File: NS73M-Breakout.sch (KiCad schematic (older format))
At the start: 5 parts, among them P1 HEADER, P2 RF_OUT, U1 NS73M, Y1 32.768 KHz

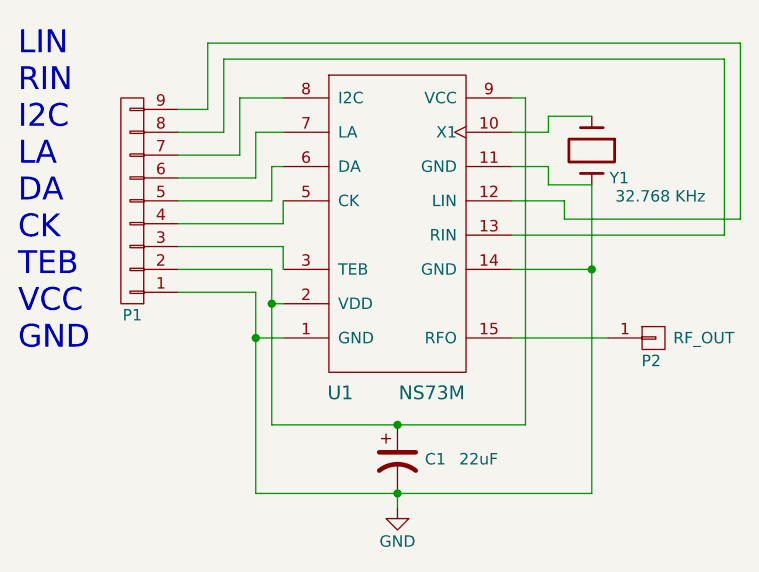
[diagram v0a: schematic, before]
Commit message: Power flags, schematic passes ERC
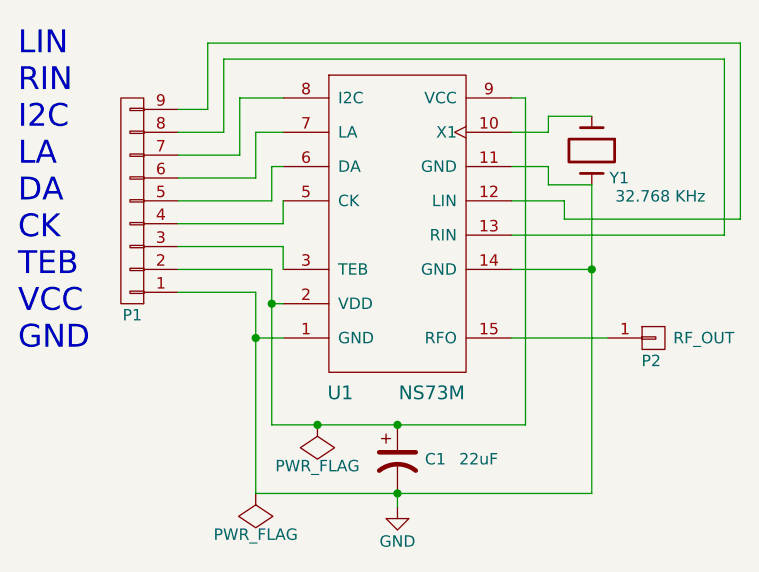
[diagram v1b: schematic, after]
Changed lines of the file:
@@
 	5050 3990 5460 3990
 Wire Wire Line
-	5460 3990 5460 4140
-Wire Wire Line
-	5460 4140 5460 4670
+	5460 3990 5460 4670
 Wire Wire Line
 	5460 4140 5510 4140
@@
 	5050 4090 5390 4090
 Wire Wire Line
-	5390 4090 5390 4290
-Wire Wire Line
-	5390 4290 5390 4970
+	5390 4090 5390 4970
 Wire Wire Line
 	5390 4290 5510 4290
 $Comp
-L GND #PWR1
+L GND #PWR01
 U 1 1 59090A59
 P 6010 5030
-F 0 "#PWR1" H 6010 4780 50  0001 C CNN
+F 0 "#PWR01" H 6010 4780 50  0001 C CNN
 F 1 "GND" H 6010 4880 50  0000 C CNN
 F 2 "" H 6010 5030 50  0000 C CNN
@@
 	6510 3990 6860 3990
 Wire Wire Line
-	6860 4970 6860 3990
-Wire Wire Line
-	6860 3990 6860 3620
+	6860 3620 6860 4970
 Connection ~ 6860 3990
 Wire Wire Line
-	5390 4970 6010 4970
-Wire Wire Line
-	6010 4970 6860 4970
-Wire Wire Line
-	5460 4670 6010 4670
-Wire Wire Line
-	6010 4670 6570 4670
+	6860 4970 5390 4970
 Connection ~ 6010 4670
 Wire Wire Line
@@
 	6010 5030 6010 4970
 Connection ~ 6010 4970
+$Comp
+L PWR_FLAG #FLG02
+U 1 1 590943D2
+P 5660 4670
+F 0 "#FLG02" H 5660 4765 50  0001 C CNN
+F 1 "PWR_FLAG" H 5660 4850 50  0000 C CNN
+F 2 "" H 5660 4670 50  0000 C CNN
+F 3 "" H 5660 4670 50  0000 C CNN
+	1    5660 4670
+	-1   0    0    1
+$EndComp
+Wire Wire Line
+	5460 4670 6570 4670
+Connection ~ 5660 4670
+$Comp
+L PWR_FLAG #FLG02
+U 1 1 590943B8
+P 5390 4970
+F 0 "#FLG02" H 5390 5065 50  0001 C CNN
+F 1 "PWR_FLAG" H 5390 5150 50  0000 C CNN
+F 2 "" H 5390 4970 50  0000 C CNN
+F 3 "" H 5390 4970 50  0000 C CNN
+	1    5390 4970
+	-1   0    0    1
+$EndComp
 $EndSCHEMATC
